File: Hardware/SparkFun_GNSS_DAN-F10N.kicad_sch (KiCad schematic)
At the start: 51 parts, among them J1 USB_C_Receptacle, J2 Conn_01x06, J4 U.FL, J5 Conn_01x09, U1 DT1042-04SO, U3 RT9080-3.3, U4 CH340C, U5 DAN-F10N

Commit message: Add ignore
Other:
- note added: "Microstrip (Coplanar Single Ended) 50Ω Calculation: https://jlcpcb.com/pcb-impedance-calculator Board thickness: 1.6mm Layers: 4 Er: 4.4 (7628 Prepreg) Dielectric Thickness (Layer 1 to 2): 8.28mil/0.2104mm (JLC7628) Copper Thickness (1oz outer / 0.5oz inner): 1.38mil/0.035mm Polygon Isolation: 7mil/0.1778mm Trace Width: 11.1mil/0.2819mm"
- note removed: "Coplanar Waveguide Calculation: Copper Thickness (1oz): 1.4mil/0.035mm Board Layers: 2 Board Thickness: 1.6mm Dielectric Thickness: 1.53mm Er: 4.6 Polygon Isolation: 6mil/0.1524mm RF Trace Width: 39mil/1.0mm https://chemandy.com/calculators/coplanar-waveguide-with-ground-calculator.htm"
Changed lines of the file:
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@@
 		)
 	)
-	(text "Coplanar Waveguide Calculation:\nCopper Thickness (1oz): 1.4mil/0.035mm\nBoard Layers: 2\nBoard Thickness: 1.6mm\nDielectric Thickness: 1.53mm\nEr: 4.6\nPolygon Isolation: 6mil/0.1524mm\nRF Trace Width: 39mil/1.0mm\nhttps://chemandy.com/calculators/coplanar-waveguide-with-ground-calculator.htm"
+	(text "Microstrip (Coplanar Single Ended) 50Ω Calculation:\nhttps://jlcpcb.com/pcb-impedance-calculator\nBoard thickness: 1.6mm\nLayers: 4\nEr: 4.4 (7628 Prepreg)\nDielectric Thickness (Layer 1 to 2): 8.28mil/0.2104mm (JLC7628)\nCopper Thickness (1oz outer / 0.5oz inner): 1.38mil/0.035mm\nPolygon Isolation: 7mil/0.1778mm\nTrace Width: 11.1mil/0.2819mm\n"
 		(exclude_from_sim no)
 		(at 250.19 166.37 0)

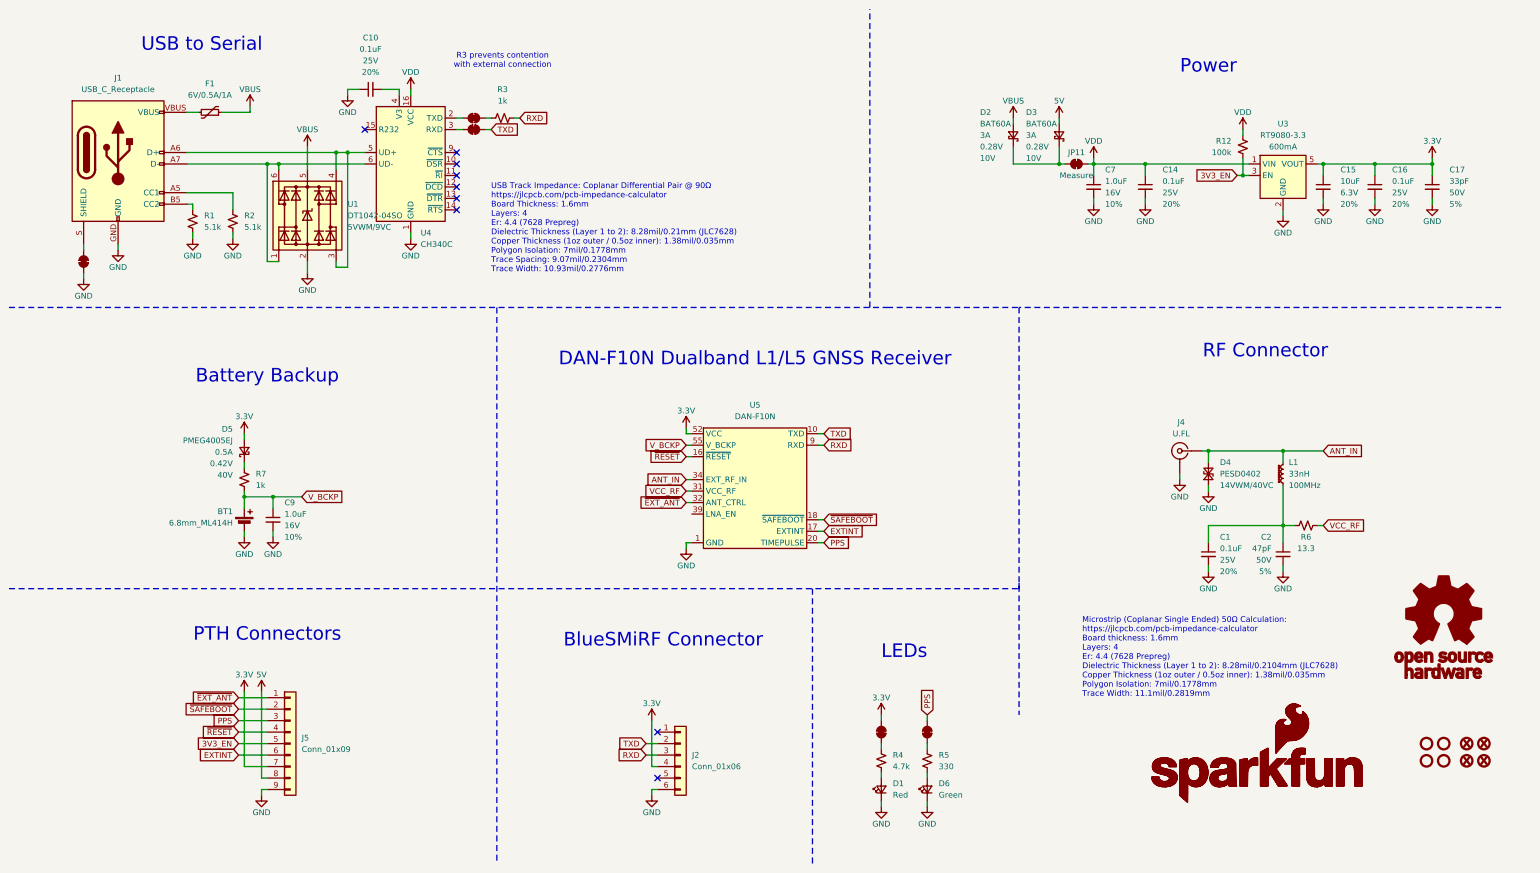
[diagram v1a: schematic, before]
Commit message: Fix DAN-F10N footprint. Move EXT_ANT to jumper.
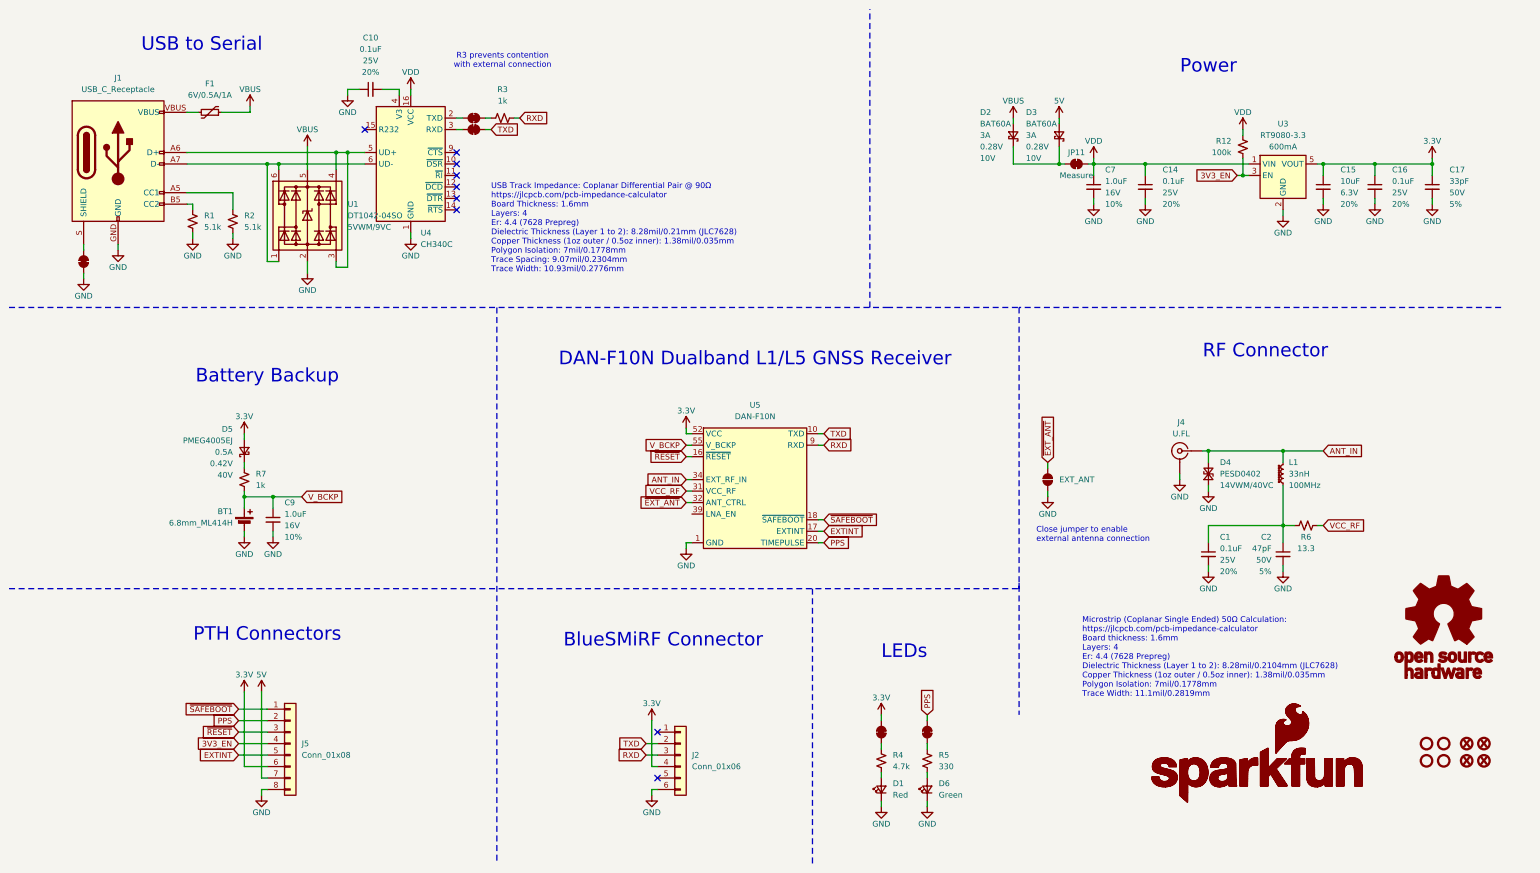
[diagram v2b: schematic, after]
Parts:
- added JP1: EXT_ANT, SparkFun-Jumper:Jumper_2_NO, symbol SparkFun-Jumper:SolderJumper_2_Open
- J5: value Conn_01x09 -> Conn_01x08; footprint SparkFun-Connector:1x09 -> SparkFun-Connector:1x08; symbol SparkFun-Connector:Conn_01x09 -> SparkFun-Connector:Conn_01x08
- R6: PROD_ID RES-... -> RES-25932
- U5: footprint Hardware:DAN-F10N -> SparkFun_GNSS_LG580P:DAN-F10N; PROD_ID GPS-... -> IC-25933
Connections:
- net 3.3V: now also J5.6 (Pin_6); no longer J5.7 (Pin_7)
- net 3V3_EN: now also J5.4 (Pin_4); no longer J5.5 (Pin_5)
- net 5V: now also J5.7 (Pin_7); no longer J5.8 (Pin_8)
- net EXTINT: now also J5.5 (Pin_5); no longer J5.6 (Pin_6)
- net GND: now also J5.8 (Pin_8), JP1.1 (A); no longer J5.9 (Pin_9)
- net PPS: now also J5.2 (Pin_2); no longer J5.3 (Pin_3)
- net ~{EXT_ANT}: now also JP1.2 (B); no longer J5.1 (Pin_1)
- net ~{RESET}: now also J5.3 (Pin_3); no longer J5.4 (Pin_4)
- net ~{SAFEBOOT}: now also J5.1 (Pin_1); no longer J5.2 (Pin_2)
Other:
- note added: "Close jumper to enable external antenna connection"
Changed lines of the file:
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@@
 	(wire
 		(pts
-			(xy 63.5 166.37) (xy 69.85 166.37)
-		)
-		(stroke
-			(width 0)
-			(type default)
-		)
-	)
-	(wire
-		(pts
 			(xy 64.77 120.65) (xy 64.77 121.92)
 		)
@@
 	(wire
 		(pts
+			(xy 242.57 120.65) (xy 242.57 121.92)
+		)
+		(stroke
+			(width 0)
+			(type default)
+		)
+	)
+	(wire
+		(pts
 			(xy 69.85 69.85) (xy 69.85 48.26)
 		)
@@
 	(wire
 		(pts
+			(xy 242.57 114.3) (xy 242.57 115.57)
+		)
+		(stroke
+			(width 0)
+			(type default)
+		)
+	)
+	(wire
+		(pts
 			(xy 163.83 132.08) (xy 162.56 132.08)
 		)
@@
 		)
 	)
+	(text "Close jumper to enable\nexternal antenna connection"
+		(exclude_from_sim no)
+		(at 240.03 132.08 0)
+		(effects
+			(font
+				(size 1.27 1.27)
+			)
+			(justify left bottom)
+		)
+	)
 	(text "R3 prevents contention\nwith external connection"
 		(exclude_from_sim no)
@@
 	(global_label "~{EXT_ANT}"
 		(shape input)
-		(at 63.5 166.37 180)
+		(at 242.57 114.3 90)
 		(fields_autoplaced yes)
 		(effects
@@
 				(size 1.27 1.27)
 			)
-			(justify right)
+			(justify left)
 		)
 		(property "Intersheetrefs" "${INTERSHEET_REFS}"
-			(at 53.4886 166.37 0)
+			(at 242.57 104.2886 90)
 			(effects
 				(font
 					(size 1.27 1.27)
 				)
-				(justify right)
+				(justify left)
 				(hide yes)
 			)
@@
 			)
 		)
-		(property "Footprint" "Hardware:DAN-F10N"
+		(property "Footprint" "SparkFun_GNSS_LG580P:DAN-F10N"
 			(at 181.61 137.16 0)
 			(effects
@@
 			)
 		)
-		(property "PROD_ID" "GPS-..."
+		(property "PROD_ID" "IC-25933"
 			(at 180.34 139.7 0)
 			(effects
@@
 	)
 	(symbol
+		(lib_id "SparkFun-Jumper:SolderJumper_2_Open")
+		(at 242.57 118.11 90)
+		(unit 1)
+		(exclude_from_sim no)
+		(in_bom yes)
+		(on_board yes)
+		(dnp no)
+		(fields_autoplaced yes)
+		(property "Reference" "JP1"
+			(at 245.11 118.11 90)
+			(effects
+				(font
+					(size 1.27 1.27)
+				)
+				(justify right)
+				(hide yes)
+			)
+		)
+		(property "Value" "EXT_ANT"
+			(at 245.11 118.11 90)
+			(effects
+				(font
+					(size 1.27 1.27)
+				)
+				(justify right)
+			)
+		)
+		(property "Footprint" "SparkFun-Jumper:Jumper_2_NO"
+			(at 245.872 118.11 0)
+			(effects
+				(font
+					(size 1.27 1.27)
+				)
+				(hide yes)
+			)
+		)
+		(property "Datasheet" "~"
+			(at 248.92 118.11 0)
+			(effects
+				(font
+					(size 1.27 1.27)
+				)
+				(hide yes)
+			)
+		)
+		(property "Description" "Solder Jumper, 2-pole, open"
+			(at 251.46 118.11 0)
+			(effects
+				(font
+					(size 1.27 1.27)
+				)
+				(hide yes)
+			)
+		)
+		(pin "1"
+		)
+		(pin "2"
+		)
+		(instances
+			(project "SparkFun_GNSS_DAN-F10N"
+				(path "/e3dd3ae4-244d-4cba-9cca-5d2abf83f29a"
+					(reference "JP1")
+					(unit 1)
+				)
+			)
+		)
+	)
+	(symbol
 		(lib_id "SparkFun-Battery:Battery_6.8mm_ML414H_IV01E")
 		(at 64.77 128.27 0)
@@
 	)
 	(symbol
+		(lib_id "SparkFun-PowerSymbol:GND")
+		(at 242.57 121.92 0)
+		(unit 1)
+		(exclude_from_sim no)
+		(in_bom yes)
+		(on_board yes)
+		(dnp no)
+		(property "Reference" "#PWR026"
+			(at 242.57 128.27 0)
+			(effects
+				(font
+					(size 1.27 1.27)
+				)
+				(hide yes)
+			)
+		)
+		(property "Value" "GND"
+			(at 242.57 125.73 0)
+			(effects
+				(font
+					(size 1.27 1.27)
+				)
+			)
+		)
+		(property "Footprint" ""
+			(at 242.57 121.92 0)
+			(effects
+				(font
+					(size 1.27 1.27)
+				)
+				(hide yes)
+			)
+		)
+		(property "Datasheet" ""
+			(at 242.57 121.92 0)
+			(effects
+				(font
+					(size 1.27 1.27)
+				)
+				(hide yes)
+			)
+		)
+		(property "Description" "Power symbol creates a global label with name \"GND\" , ground"
+			(at 242.57 130.81 0)
+			(effects
+				(font
+					(size 1.27 1.27)
+				)
+				(hide yes)
+			)
+		)
+		(pin "1"
+		)
+		(instances
+			(project "SparkFun_GNSS_DAN-F10N"
+				(path "/e3dd3ae4-244d-4cba-9cca-5d2abf83f29a"
+					(reference "#PWR026")
+					(unit 1)
+				)
+			)
+		)
+	)
+	(symbol
 		(lib_id "SparkFun-Hardware:Standoff")
 		(at 326.39 176.53 0)
@@
 			)
 		)
-		(property "PROD_ID" "RES-..."
+		(property "PROD_ID" "RES-25932"
 			(at 299.72 121.412 0)
 			(effects
@@
 	)
 	(symbol
-		(lib_id "SparkFun-Connector:Conn_01x09")
+		(lib_id "SparkFun-Connector:Conn_01x08")
 		(at 74.93 176.53 0)
 		(unit 1)
@@
 		(fields_autoplaced yes)
 		(property "Reference" "J5"
-			(at 77.47 175.2599 0)
+			(at 77.47 176.5299 0)
 			(effects
 				(font
@@
 			)
 		)
-		(property "Value" "Conn_01x09"
-			(at 77.47 177.7999 0)
+		(property "Value" "Conn_01x08"
+			(at 77.47 179.0699 0)
 			(effects
 				(font
@@
 			)
 		)
-		(property "Footprint" "SparkFun-Connector:1x09"
+		(property "Footprint" "SparkFun-Connector:1x08"
 			(at 74.93 191.77 0)
 			(effects
@@
 		(pin "2"
 		)
-		(pin "9"
-		)
 		(pin "8"

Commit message: Fix standoff location. Update to v9.
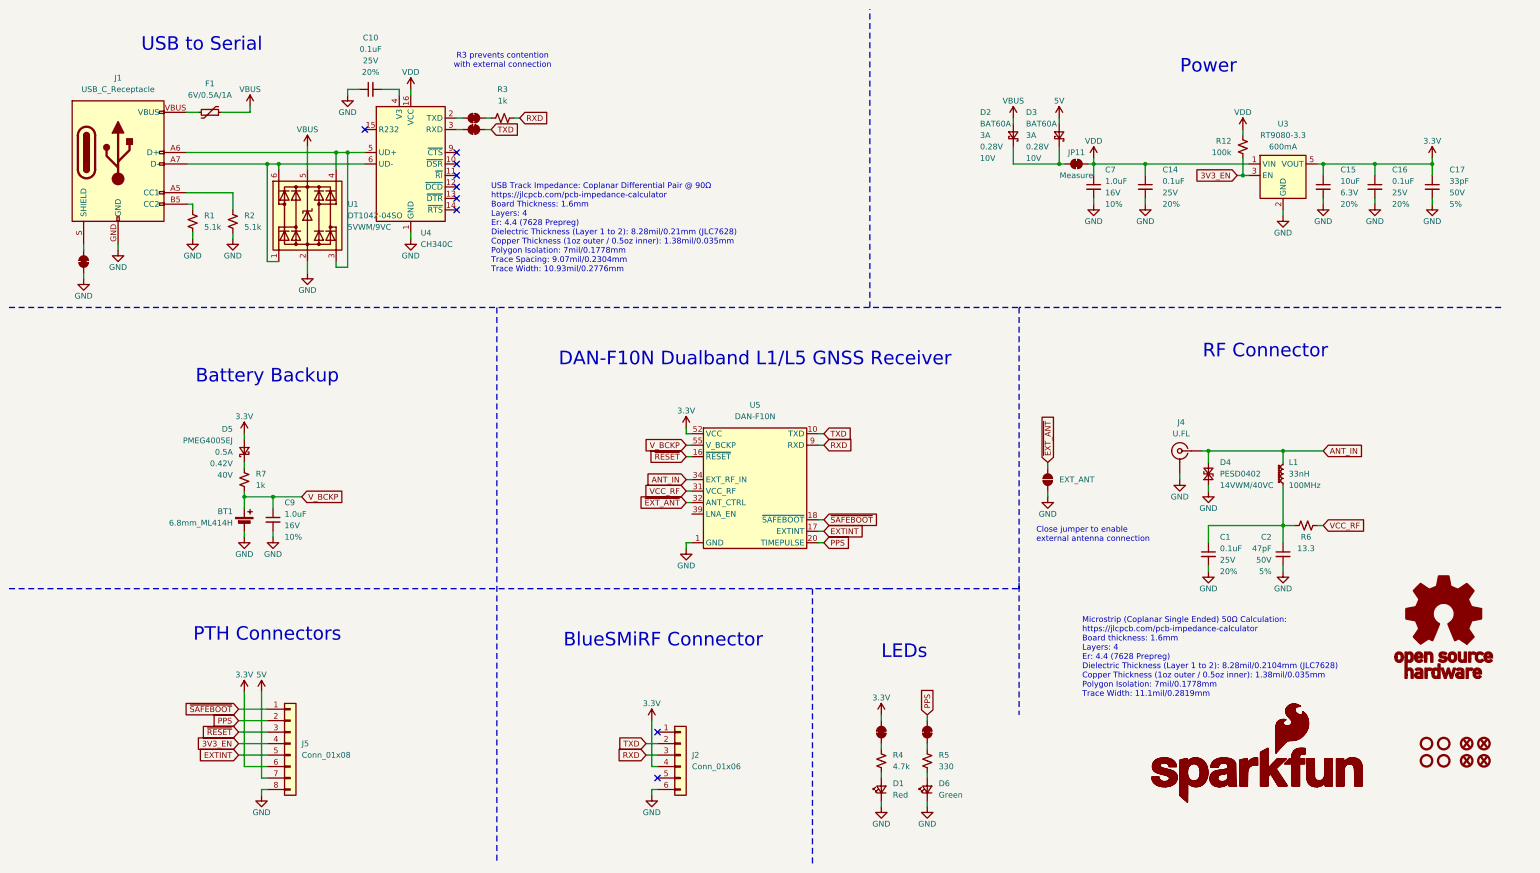
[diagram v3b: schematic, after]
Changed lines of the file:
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@@
 (kicad_sch
-	(version 20231120)
+	(version 20250114)
 	(generator "eeschema")
-	(generator_version "8.0")
+	(generator_version "9.0")
 	(paper "USLegal")
 	(title_block
@@
 		(comment 1 "Designed by: N. Seidle")
 	)
+	(text "Close jumper to enable\nexternal antenna connection"
+		(exclude_from_sim no)
+		(at 240.03 132.08 0)
+		(effects
+			(font
+				(size 1.27 1.27)
+			)
+			(justify left bottom)
+		)
+	)
+	(text "R3 prevents contention\nwith external connection"
+		(exclude_from_sim no)
+		(at 121.92 25.4 0)
+		(effects
+			(font
+				(size 1.27 1.27)
+			)
+		)
+	)
+	(text "Microstrip (Coplanar Single Ended) 50Ω Calculation:\nhttps://jlcpcb.com/pcb-impedance-calculator\nBoard thickness: 1.6mm\nLayers: 4\nEr: 4.4 (7628 Prepreg)\nDielectric Thickness (Layer 1 to 2): 8.28mil/0.2104mm (JLC7628)\nCopper Thickness (1oz outer / 0.5oz inner): 1.38mil/0.035mm\nPolygon Isolation: 7mil/0.1778mm\nTrace Width: 11.1mil/0.2819mm\n"
+		(exclude_from_sim no)
+		(at 250.19 166.37 0)
+		(effects
+			(font
+				(size 1.27 1.27)
+			)
+			(justify left bottom)
+		)
+	)
+	(text "USB Track Impedance: Coplanar Differential Pair @ 90Ω\nhttps://jlcpcb.com/pcb-impedance-calculator\nBoard Thickness: 1.6mm\nLayers: 4\nEr: 4.4 (7628 Prepreg)\nDielectric Thickness (Layer 1 to 2): 8.28mil/0.21mm (JLC7628) \nCopper Thickness (1oz outer / 0.5oz inner): 1.38mil/0.035mm\nPolygon Isolation: 7mil/0.1778mm\nTrace Spacing: 9.07mil/0.2304mm\nTrace Width: 10.93mil/0.2776mm"
+		(exclude_from_sim no)
+		(at 119.38 72.39 0)
+		(effects
+			(font
+				(size 1.27 1.27)
+			)
+			(justify left bottom)
+		)
+	)
+	(text "RF Connector"
+		(exclude_from_sim no)
+		(at 276.86 91.44 0)
+		(effects
+			(font
+				(size 3 3)
+			)
+			(justify left bottom)
+		)
+	)
+	(text "BlueSMiRF Connector"
+		(exclude_from_sim no)
+		(at 157.48 153.67 0)
+		(effects
+			(font
+				(size 3 3)
+			)
+		)
+	)
+	(text "LEDs\n"
+		(exclude_from_sim no)
+		(at 210.82 156.21 0)
+		(effects
+			(font
+				(size 3 3)
+			)
+		)
+	)
+	(text "DAN-F10N Dualband L1/L5 GNSS Receiver"
+		(exclude_from_sim no)
+		(at 177.8 91.44 0)
+		(effects
+			(font
+				(size 3 3)
+			)
+		)
+	)
+	(text "USB to Serial"
+		(exclude_from_sim no)
+		(at 55.372 21.844 0)
+		(effects
+			(font
+				(size 3 3)
+			)
+		)
+	)
+	(text "Battery Backup"
+		(exclude_from_sim no)
+		(at 69.85 95.25 0)
+		(effects
+			(font
+				(size 3 3)
+			)
+		)
+	)
+	(text "Power\n"
+		(exclude_from_sim no)
+		(at 278.13 26.67 0)
+		(effects
+			(font
+				(size 3 3)
+			)
+		)
+	)
+	(text "PTH Connectors"
+		(exclude_from_sim no)
+		(at 69.85 152.4 0)
+		(effects
+			(font
+				(size 3 3)
+			)
+		)
+	)
 	(junction
 		(at 87.63 45.72)
@@
 		)
 	)
-	(text "Close jumper to enable\nexternal antenna connection"
-		(exclude_from_sim no)
-		(at 240.03 132.08 0)
-		(effects
-			(font
-				(size 1.27 1.27)
-			)
-			(justify left bottom)
-		)
-	)
-	(text "R3 prevents contention\nwith external connection"
-		(exclude_from_sim no)
-		(at 121.92 25.4 0)
-		(effects
-			(font
-				(size 1.27 1.27)
-			)
-		)
-	)
-	(text "Microstrip (Coplanar Single Ended) 50Ω Calculation:\nhttps://jlcpcb.com/pcb-impedance-calculator\nBoard thickness: 1.6mm\nLayers: 4\nEr: 4.4 (7628 Prepreg)\nDielectric Thickness (Layer 1 to 2): 8.28mil/0.2104mm (JLC7628)\nCopper Thickness (1oz outer / 0.5oz inner): 1.38mil/0.035mm\nPolygon Isolation: 7mil/0.1778mm\nTrace Width: 11.1mil/0.2819mm\n"
-		(exclude_from_sim no)
-		(at 250.19 166.37 0)
-		(effects
-			(font
-				(size 1.27 1.27)
-			)
-			(justify left bottom)
-		)
-	)
-	(text "USB Track Impedance: Coplanar Differential Pair @ 90Ω\nhttps://jlcpcb.com/pcb-impedance-calculator\nBoard Thickness: 1.6mm\nLayers: 4\nEr: 4.4 (7628 Prepreg)\nDielectric Thickness (Layer 1 to 2): 8.28mil/0.21mm (JLC7628) \nCopper Thickness (1oz outer / 0.5oz inner): 1.38mil/0.035mm\nPolygon Isolation: 7mil/0.1778mm\nTrace Spacing: 9.07mil/0.2304mm\nTrace Width: 10.93mil/0.2776mm"
-		(exclude_from_sim no)
-		(at 119.38 72.39 0)
-		(effects
-			(font
-				(size 1.27 1.27)
-			)
-			(justify left bottom)
-		)
-	)
-	(text "RF Connector"
-		(exclude_from_sim no)
-		(at 276.86 91.44 0)
-		(effects
-			(font
-				(size 3 3)
-			)
-			(justify left bottom)
-		)
-	)
-	(text "BlueSMiRF Connector"
-		(exclude_from_sim no)
-		(at 157.48 153.67 0)
-		(effects
-			(font
-				(size 3 3)
-			)
-		)
-	)
-	(text "LEDs\n"
-		(exclude_from_sim no)
-		(at 210.82 156.21 0)
-		(effects
-			(font
-				(size 3 3)
-			)
-		)
-	)
-	(text "DAN-F10N Dualband L1/L5 GNSS Receiver"
-		(exclude_from_sim no)
-		(at 177.8 91.44 0)
-		(effects
-			(font
-				(size 3 3)
-			)
-		)
-	)
-	(text "USB to Serial"
-		(exclude_from_sim no)
-		(at 55.372 21.844 0)
-		(effects
-			(font
-				(size 3 3)
-			)
-		)
-	)
-	(text "Battery Backup"
-		(exclude_from_sim no)
-		(at 69.85 95.25 0)
-		(effects
-			(font
-				(size 3 3)
-			)
-		)
-	)
-	(text "Power\n"
-		(exclude_from_sim no)
-		(at 278.13 26.67 0)
-		(effects
-			(font
-				(size 3 3)
-			)
-		)
-	)
-	(text "PTH Connectors"
-		(exclude_from_sim no)
-		(at 69.85 152.4 0)
-		(effects
-			(font
-				(size 3 3)
-			)
-		)
-	)
 	(global_label "RXD"
 		(shape input)
@@
 		)
 	)
+	(embedded_fonts no)
 )
